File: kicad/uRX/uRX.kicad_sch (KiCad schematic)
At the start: 133 parts, among them J1 RF_AM_GND, J10 GPIO_A, J2 C165948, J3 AudioJack2_Ground, J4 Display, J6 U.FL, J9 RF_AM__In, Q1 BC847, SW1 RotaryEncoder_Switch, SW2 SW_DPDT_x2, SW3 Reset, SW4 Boot, U1 CBT3253, U10 IP2326, U11 LP2985-5.0, U12 OPA2211, U13 HT733333, U2 LM4562, U4 Si5351A-B-GT, U5 ESP32-S3-WROOM-2, U6 Si4732-A10, U7 PCM1808PWR, U8 LM4040-2.5, U9 PCM1808PWR, X1 X322525MOB4SI, Y2 32768kHz

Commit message: add audio amp
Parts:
- removed J3: AudioJack2_Ground, Connector_Audio:Jack_3.5mm_CUI_SJ1-3523N_Horizontal, symbol Connector_Audio:AudioJack2_Ground
- added C39: 1u, Capacitor_SMD:C_0603_1608Metric, symbol uRX:C_Small
- added C47, C48: 1u, Capacitor_SMD:C_0603_1608Metric, symbol Device:C_Small
- added C49: 10u, Capacitor_SMD:C_0603_1608Metric, symbol uRX:C_Small
- added C50, C51: 100n, Capacitor_SMD:C_0603_1608Metric, symbol uRX:C_Small
- added R23: 10, Resistor_SMD:R_0603_1608Metric, symbol uRX:R
- added R24, R25: 1k, Resistor_SMD:R_0603_1608Metric, symbol uRX:R
- added U3: PAM8406D, Package_SO:SOIC-16_3.9x9.9mm_P1.27mm, symbol Amplifier_Audio:PAM8406D
- C17, C18: value 4.7u -> 1u
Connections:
- net +3.3V: now also C49.2, C50.2, R23.1, U3.13 (PVDDR), U3.4 (PVDDL), U3.9 (MODE)
- net GND: now also C39.1, C49.1, C50.1, C51.1, U3.11 (GND), U3.15 (PGNDR), U3.2 (PGNDL)
- net Q_BAT_STAT: now also U5.24 (GPIO47/SPICLK_P/SUBSPICLK_P_DIFF); no longer U5.25 (GPIO48/SPICLK_N/SUBSPICLK_N_DIFF)
- net at SW2.1 (A): no longer U11.5 (VOUT)
- net at SW2.3 (C): now also U11.5 (VOUT)
- net at U6.1 (LOut): now also C18.1, C48.2; no longer C17.2
- net at U6.16 (ROut): now also C17.1, C47.2; no longer C18.2
- net at U9.14 (VINR): now also C18.2; no longer C17.1
- net AUDIO_MUTE: now reaches U5.26 (GPIO45)
- net AUDIO_MUTE: now also U3.5 (~{MUTE})
- net at U9.13 (VINL): now also C17.2; no longer C18.1
- new net: C51.2, R23.2, U3.6 (VDD)
- new net: C39.2, U3.8 (VREF)
- new net: R25.1, U3.10 (INR)
- new net: R24.1, U3.7 (INL)
- new net AUDIO_IN_L: C48.1, R24.2
- new net AUDIO_IN_R: C47.1, R25.2
- new net AUDIO_OUT_L+: U3.1 (+OUT_L)
- new net AUDIO_OUT_L-: U3.3 (-OUT_L)
- new net AUDIO_OUT_R+: U3.16 (+OUT_R)
- new net AUDIO_OUT_R-: U3.14 (-OUT_R)
- new net AUDIO_SHND: U3.12 (~{SHND}), U5.25 (GPIO48/SPICLK_N/SUBSPICLK_N_DIFF)
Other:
- moved on the sheet: C17, C18

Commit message: split stero-mono
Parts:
- removed Bat2, Bat3: JST-XH, Connector_JST:JST_XH_B3B-XH-A_1x03_P2.50mm_Vertical, symbol uRX:Conn_01x03
- added C52: 1u, Capacitor_SMD:C_0603_1608Metric, symbol Device:C_Small
- added C53: 10n, Capacitor_SMD:C_0603_1608Metric, symbol uRX:C_Small
- added C54: 1u, Capacitor_SMD:C_0603_1608Metric, symbol uRX:C_Small
- added J3: Loudspeaker, Connector_JST:JST_PH_B2B-PH-K_1x02_P2.00mm_Vertical, symbol Connector_Generic:Conn_01x02
- added J5: BAT0, JST_PH_B3B-PH-K_1x03_P2.00mm_Vertical, symbol Connector_Generic:Conn_01x03
- added J7: BAT1, JST_PH_B3B-PH-K_1x03_P2.00mm_Vertical, symbol Connector_Generic:Conn_01x03
- added R31, R32: 1k, Resistor_SMD:R_0603_1608Metric, symbol Device:R
- added Rf8: 47, Resistor_SMD:R_0603_1608Metric, symbol Device:R
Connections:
- net +VBatt: now also J5.3 (Pin_3), J7.3 (Pin_3)
- net GND: now also C53.1, C54.1, J5.1 (Pin_1), J7.1 (Pin_1)
- net at R39.2: now also J5.2 (Pin_2), J7.2 (Pin_2)
- net at U4.6 (CLK2): now also Rf1.1, TP6.1, Rf8.1; no longer Rf1.2
- net AUDIO_MONO_4732: now reaches R25.1, U3.10 (INR)
- net AUDIO_MONO_4732: now also R31.1, R32.1
- net at R24.1: now also C52.1, C53.2; no longer U3.7 (INL)
- removed net ADC_SCKI: J10.3 (Pin_3), Rf1.1, TP6.1, U5.18 (GPIO10/TOUCH10/ADC1_CH9/FSPICS0/FSPIIO4/SUBSPICS0), U7.6 (SCKI), U9.6 (SCKI)
- net AUDIO_IN_L: no longer names the net of C48.1
- net AUDIO_IN_L: now also R32.2; no longer R24.2
- net AUDIO_IN_R: no longer names the net of R25.2
- net AUDIO_IN_R: now also C52.2; no longer C47.1
- net AUDIO_OUT_L+: no longer names the net of U3.1 (+OUT_L)
- net AUDIO_OUT_L+: now also J3.1 (Pin_1)
- net AUDIO_OUT_L-: no longer names the net of U3.3 (-OUT_L)
- net AUDIO_OUT_L-: now also J3.2 (Pin_2)
- net AUDIO_OUT_R+: no longer names the net of U3.16 (+OUT_R)
- net AUDIO_OUT_R-: no longer names the net of U3.14 (-OUT_R)
- new net: C47.1, R31.2
- new net: C54.2, U3.7 (INL)
- new net ADC0_SCKI: Rf8.2, U7.6 (SCKI)
- new net ADC1_SCKI: Rf1.2, U9.6 (SCKI)
- new net AUDIO_MONO_ESP: J10.3 (Pin_3), R24.2, U5.18 (GPIO10/TOUCH10/ADC1_CH9/FSPICS0/FSPIIO4/SUBSPICS0)
- no-connect marks 4 -> 6
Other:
- moved on the sheet: C48, C49, C50, C51, R24

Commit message: all lines connected
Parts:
- added L5: L_Core_Ferrite, Inductor_SMD:L_Taiyo-Yuden_NR-40xx, symbol Device:L_Ferrite_Small
- added NT1, NT2: NetTie_2, NetTie:NetTie-2_SMD_Pad0.5mm, symbol Device:NetTie_2
- added unit 3 of U2
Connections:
- net +5Vfiltered: now also U2.8 (V+)
- net Earth: now also NT1.1; no longer U6.7 (RFGND)
- net GND: now also NT1.2, NT2.2, U2.4 (V-)
- net USB_D+: now also U10.2 (DP)
- net USB_D-: now also U10.1 (DM)
- net VBUS: now also L5.2; no longer J2.A4 (VBUS), J2.A9 (VBUS), J2.B4 (VBUS), J2.B9 (VBUS)
- new net: NT2.1, U6.7 (RFGND)
- new net: J2.A4 (VBUS), J2.A9 (VBUS), J2.B4 (VBUS), J2.B9 (VBUS), L5.1
- no-connect marks 6 -> 18
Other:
- moved on the sheet: C10, C11

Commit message: work on power lines
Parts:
- removed J5: BAT0, JST_PH_B3B-PH-K_1x03_P2.00mm_Vertical, symbol Connector_Generic:Conn_01x03
- removed J7: BAT1, JST_PH_B3B-PH-K_1x03_P2.00mm_Vertical, symbol Connector_Generic:Conn_01x03
- added C55, C56, C57: 10u, C_0805_2012Metric, symbol uRX:C_Small
- added J11: Bat1, Connector_JST:JST_PH_B2B-PH-K_1x02_P2.00mm_Vertical, symbol Connector_Generic:Conn_01x02
- added J8: Bat0, Connector_JST:JST_PH_B2B-PH-K_1x02_P2.00mm_Vertical, symbol Connector_Generic:Conn_01x02
- added L6: L_Core_Ferrite, Inductor_SMD:L_Taiyo-Yuden_NR-40xx, symbol Device:L_Ferrite_Small
- C34: footprint Capacitor_SMD:C_0603_1608Metric -> C_0805_2012Metric
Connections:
- net +VBatt: now also C57.2, J8.2 (Pin_2), L6.1; no longer U10.21 (VOUT), U10.22 (VOUT)
- net GND: now also C55.1, C56.1, C57.1, J11.1 (Pin_1)
- net at J2.A4 (VBUS), J2.A9 (VBUS), J2.B4 (VBUS)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: now also L5.2, C55.2; no longer L5.1
- net at R21.2, SW1.A, U5.32 (MTCK/GPIO39/CLK_OUT3/SUBSPICS1): now also C46.2; no longer C45.2
- net at R22.2, SW1.B, U5.33 (MTDO/GPIO40/CLK_OUT2): now also C45.2; no longer C46.2
- net at R39.2: now also J11.2 (Pin_2), J8.1 (Pin_1)
- net VBUS renamed VBUSfiltered
- net VBUSfiltered: now also L5.1; no longer L5.2
- new net: C56.2, L6.2, U10.21 (VOUT), U10.22 (VOUT)
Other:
- moved on the sheet: C39, C49, C50, C51, C52, C53, C54, D5, J3, L5, R21, R22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

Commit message: seafile corruption
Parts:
- added L7: Ferrite_perl, Inductor_SMD:L_0603_1608Metric, symbol Device:L_Ferrite_Small
- C2, C3, C4: value 220n -> 470n
- C5: value 220n -> 470
- C6, C7: value 1.2n -> 5.6n
- R10, R11, R12, R8: value 1k -> 100
- R18, R19, R3, R4: value 47k -> 10k
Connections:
- net +3.3V: no longer C30.2, R5.1, U6.14 (VDD), U9.4 (VDD)
- net +5V: now also L7.1; no longer C29.2, C31.2, U9.1 (VREF), U9.3 (VCC)
- net at C5.1, R10.2: now also U1.13 (2B4), U1.3 (1B4); no longer U1.12 (2B3), U1.4 (1B3)
- net at C3.1, R8.2: now also U1.12 (2B3), U1.4 (1B3); no longer U1.13 (2B4), U1.3 (1B4)
- net +3.3Vfiltered renamed +3.3VfilteredM
- net +3.3VfilteredM: now also C30.2, R5.1, U6.14 (VDD), U9.4 (VDD); no longer J10.11 (Pin_11)
- net +5Vfiltered renamed +5VfilteredQ
- net +5VfilteredQ: no longer C20.2, C28.2, J10.12 (Pin_12), U7.1 (VREF), U7.3 (VCC)
- new net +5VfilteredM: C20.2, C28.2, C29.2, C31.2, L7.2, U7.1 (VREF), U7.3 (VCC), U9.1 (VREF), U9.3 (VCC)
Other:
- note added: "I"
- note added: "Q"

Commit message: correct taylo
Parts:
- added JP1: AudioMix, Connector_PinHeader_2.54mm:PinHeader_1x02_P2.54mm_Vertical, symbol Jumper:Jumper_2_Open
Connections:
- net AUDIO_MONO_4732: now also JP1.2 (B); no longer R25.1, U3.10 (INR)
- net at J3.1 (Pin_1): now also U3.16 (+OUT_R); no longer U3.1 (+OUT_L)
- net at J3.2 (Pin_2): now also U3.14 (-OUT_R); no longer U3.3 (-OUT_L)
- new net: JP1.1 (A), R25.1, U3.10 (INR)
- no-connect marks 18 -> 16
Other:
- moved on the sheet: C24, C25, C32, C44, C45, C46, D2, D5, J10, J3, J4, L1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

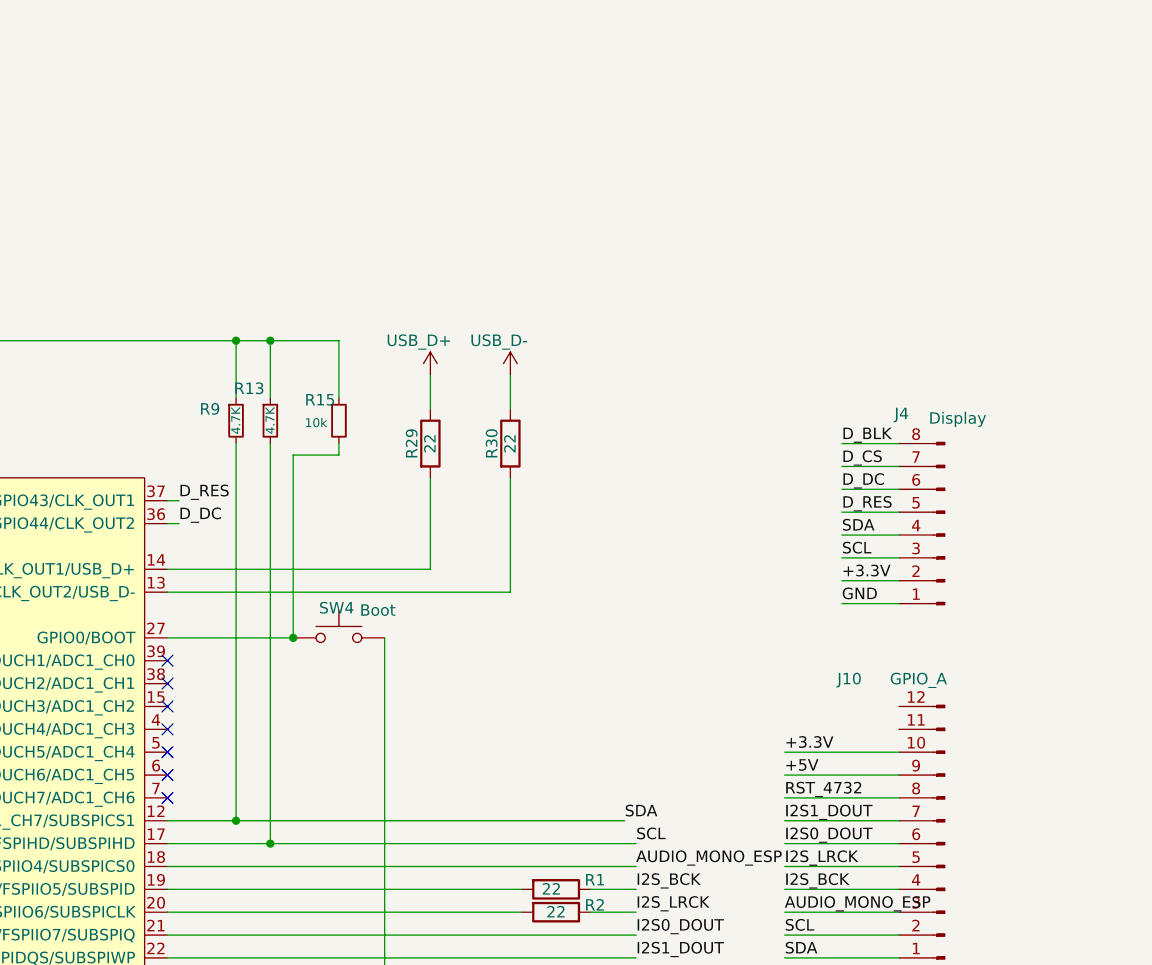
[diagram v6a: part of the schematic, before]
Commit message: add e-inc wiring
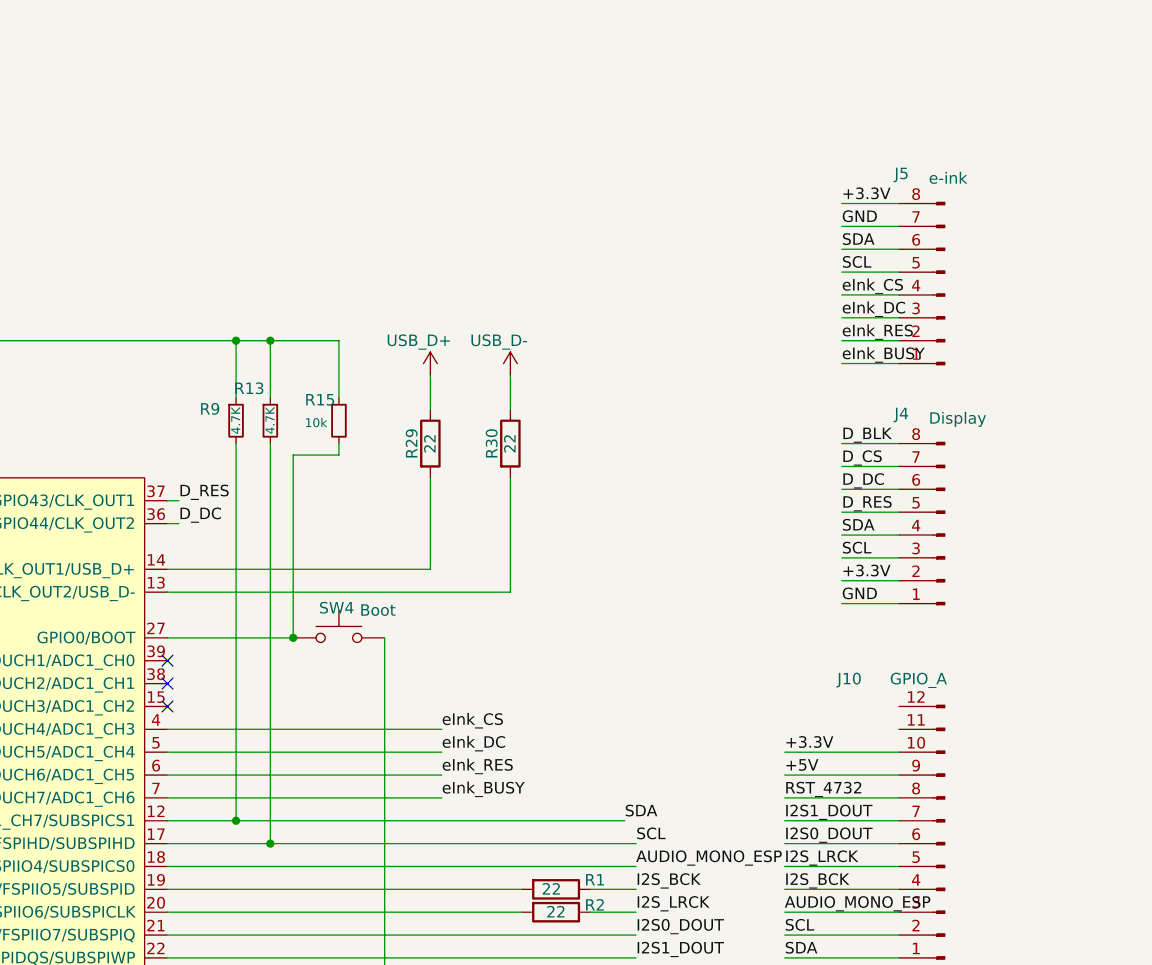
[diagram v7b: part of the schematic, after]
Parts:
- added J5: e-ink, PinHeader_1x08_P1.27mm_Horizontal, symbol Connector:Conn_01x08_Pin
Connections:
- net +3.3V: now also J5.8 (Pin_8)
- net GND: now also J5.7 (Pin_7)
- net SCL: now also J5.5 (Pin_5)
- net SDA: now also J5.6 (Pin_6)
- net eInk_CS: now reaches U5.4 (GPIO4/TOUCH4/ADC1_CH3)
- net eInk_CS: now also J5.4 (Pin_4)
- net eInk_DC: now reaches U5.5 (GPIO5/TOUCH5/ADC1_CH4)
- net eInk_DC: now also J5.3 (Pin_3)
- net eInk_RES: now reaches U5.6 (GPIO6/TOUCH6/ADC1_CH5)
- net eInk_RES: now also J5.2 (Pin_2)
- net eInk_BUSY: now reaches U5.7 (GPIO7/TOUCH7/ADC1_CH6)
- net eInk_BUSY: now also J5.1 (Pin_1)
- no-connect marks 16 -> 12

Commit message: feels like the schematics/pcb is complete
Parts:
- added R33, R45: 4.7K, Resistor_SMD:R_0603_1608Metric, symbol Device:R_Small
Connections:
- net GND is gone; now on net +5VfilteredM: C10.2, C11.2, C13.2, C14.2, C19.1, C2.2, C20.1, C21.1, C22.1, C23.1, C24.2, C25.2, C26.2, C27.2, C28.1, C29.1, C3.2, C30.1, C31.1, C32.2, C34.2, C36.2, C37.2, C39.1, C4.2, C40.2, C41.2, C43.2, C44.2, C45.1, C46.1, C49.1, C5.2, C50.1, C51.1, C53.1, C54.1, C55.1, C56.1, C57.1, C8.2, C9.2, D3.1 (K), D4.1 (K), D6.2 (A), J1.1 (Pin_1), J11.1 (Pin_1), J2.A1 (GND), J2.A12 (GND), J2.B1 (GND), J2.B12 (GND), J4.1 (Pin_1), J5.7 (Pin_7), J6.2 (Ext), NT1.2, NT2.2, Q1.2 (E), R34.2, R35.2, R36.2, R37.2, R41.2, R42.2, R43.2, R44.2, SW1.C, SW1.S2, SW3.1, SW4.2, U1.1 (1~{OE}), U1.15 (2~{OE}), U1.8 (GND), U10.18 (PGND), U10.24 (VBAT_GND), U11.2 (GND), U12.4 (V-), U13.2 (GND), U2.4 (V-), U3.11 (GND), U3.15 (PGNDR), U3.2 (PGNDL), U4.8 (GND), U5.1 (GND), U5.40 (GND), U5.41 (GND), U6.10 (SENB), U6.15 (GND), U7.10 (MD0), U7.11 (MD1), U7.12 (FMT), U7.2 (AGND), U7.5 (DGND), U8.2 (A), U9.10 (MD0), U9.11 (MD1), U9.12 (FMT), U9.2 (AGND), U9.5 (DGND), X1.2 (GND), X1.4 (GND)
- net +3.3V: now also R33.1, R45.1
- net eInk_CS: now also R45.2
- net eInk_RES: now also R33.2
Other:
- note added: "Audio Output Amplifier"
- note added: "Battery Charge and USB interface"
- note added: "Voltage Regulators"
- moved on the sheet: 2211Out1, C1, C10, C11, C12, C13, C14, C15, C16, C17, C18, C19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
